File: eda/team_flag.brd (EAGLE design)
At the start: 40.6 x 40.6 mm, 28 parts, among them Q1 IRFML8244, Q2 IRFML8244, U1 ISL83491SOIC, U2 ATTINY1634

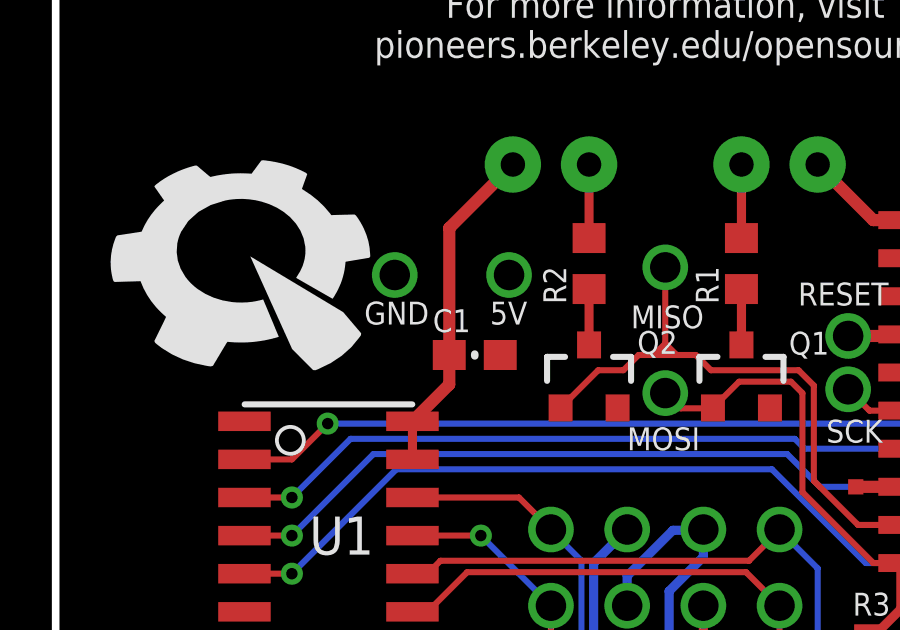
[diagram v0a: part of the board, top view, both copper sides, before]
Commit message: Replaced 2x4 connectors with 2x5's.
On smartsensor, smartsensorPowered, smartsensor_powered_jig, and team_flag.
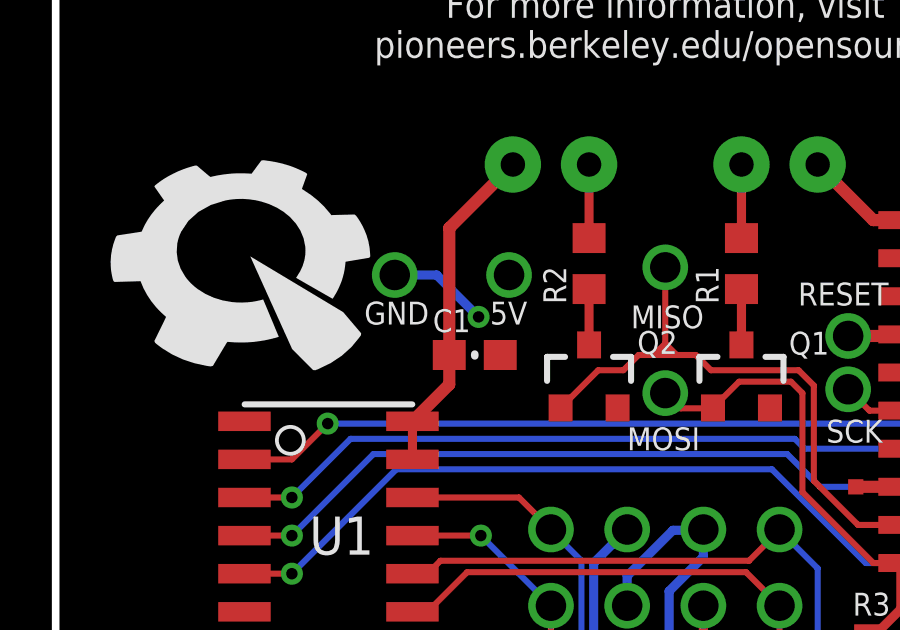
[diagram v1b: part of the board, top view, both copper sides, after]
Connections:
- net 5V: now also 5V.POGO_PIN
- net GND: now also GND.POGO_PIN
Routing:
- net GND: track 11.4 -> 14.9 mm, vias 0 -> 1
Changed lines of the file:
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@@
 <wire x1="17.018" y1="8.128" x2="18.0086" y2="8.128" width="0.3048" layer="16"/>
 <wire x1="18.0086" y1="8.128" x2="18.034" y2="8.1534" width="0.3048" layer="16"/>
-<wire x1="18.034" y1="2.794" x2="25.2594" y2="4.445" width="0" layer="19" extent="1-16"/>
+<contactref element="GND" pad="POGO_PIN"/>
+<wire x1="11.264" y1="13.97" x2="11.43" y2="13.97" width="0.3048" layer="1"/>
+<via x="10.541" y="15.24" extent="1-16" drill="0.381"/>
+<wire x1="7.747" y1="16.637" x2="9.144" y2="16.637" width="0.3048" layer="16"/>
+<wire x1="9.144" y1="16.637" x2="10.541" y2="15.24" width="0.3048" layer="16"/>
 </signal>
 <signal name="BLUE">
@@
 <wire x1="14.3764" y1="4.2672" x2="14.4018" y2="4.2926" width="0.3048" layer="16"/>
 <wire x1="14.3764" y1="7.0358" x2="15.494" y2="8.1534" width="0.3048" layer="16"/>
+<contactref element="5V" pad="POGO_PIN"/>
 </signal>
 <signal name="TX">

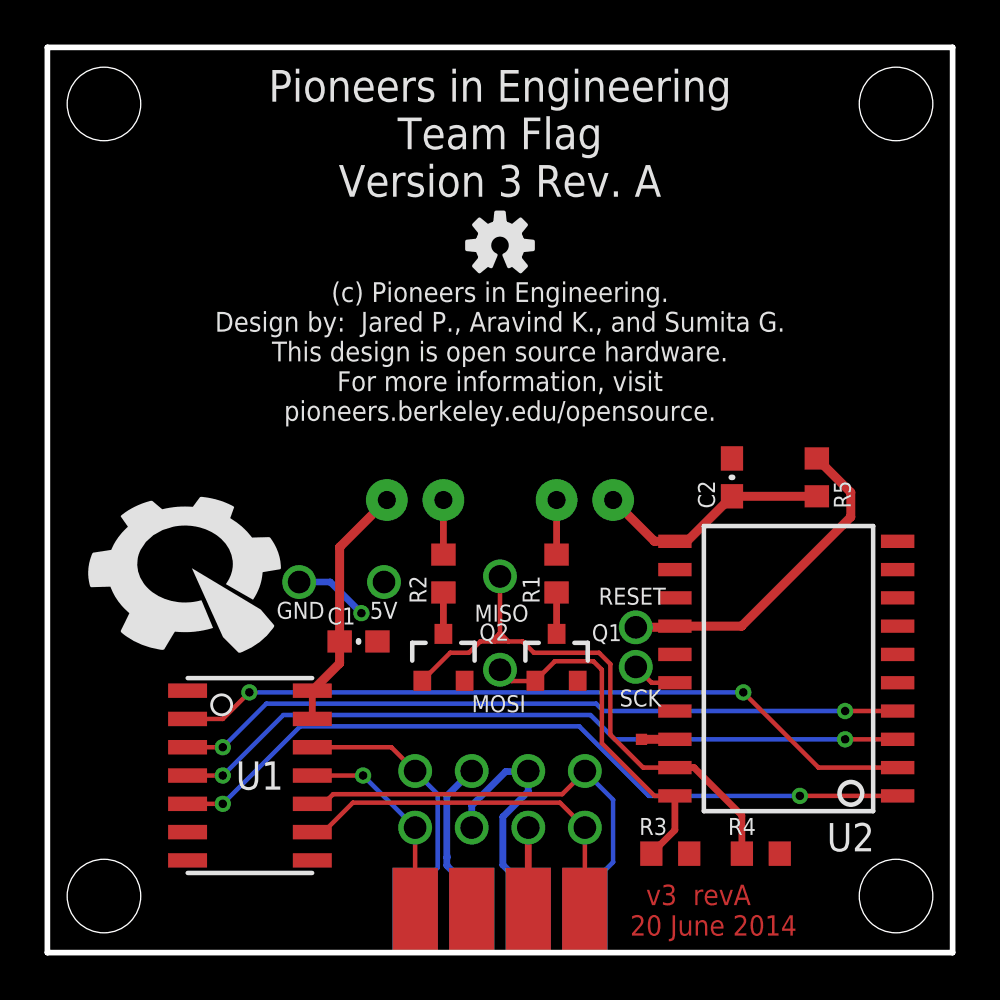
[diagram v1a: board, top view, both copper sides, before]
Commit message: Replaced 2x4 connector with 2x5 on team_flag.
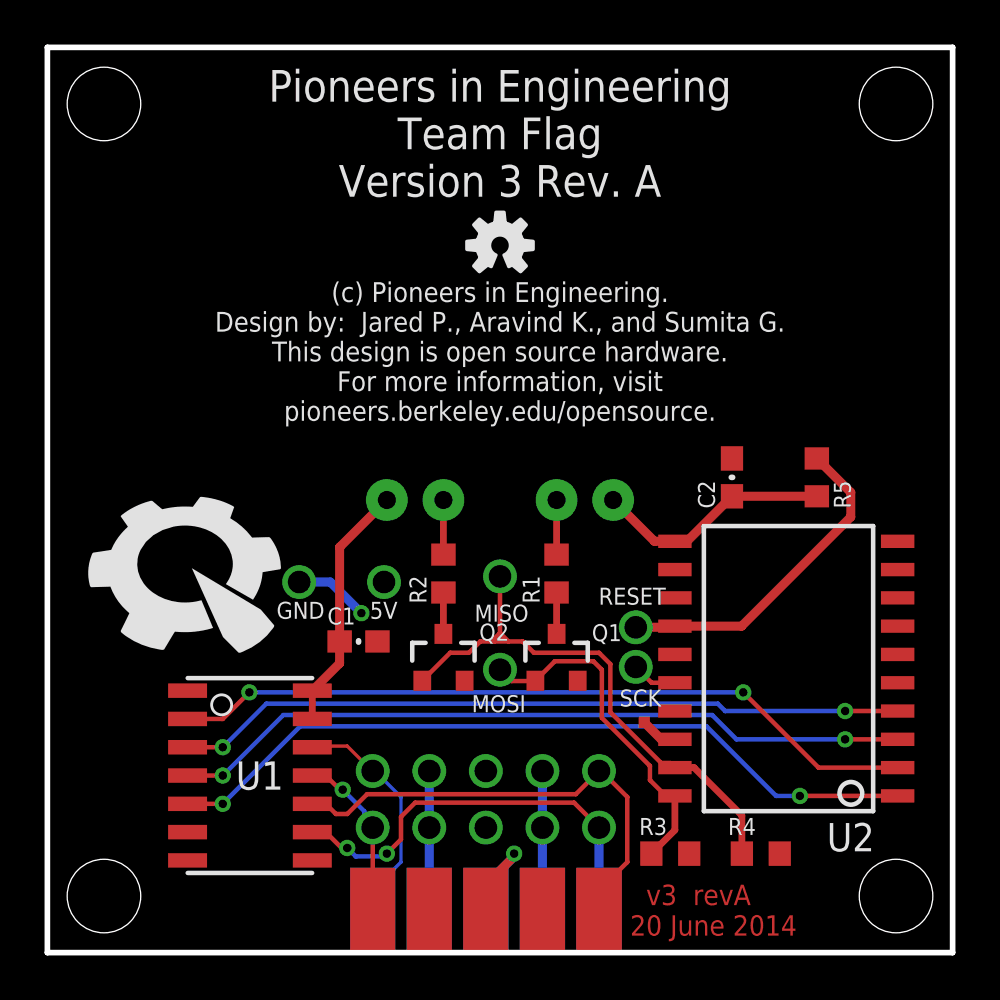
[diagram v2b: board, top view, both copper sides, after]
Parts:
- U$8: value SENSOR_CONPTH -> (none); device pie:2X4 -> pie:2X5
- U$9: value SENSOR_CONSMD-EDGE -> (none); device pie:2X4-EDGE -> pie:2X5-EDGE
- moved TP3 0.77 mm to (23.2, 10.3)
- moved U$8 0.63 mm to (16.1, 6.88)
- moved U$9 0.63 mm to (16.1, -0.64)
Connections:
- net 5V: now also U$8.5, U$9.5; no longer U$8.3, U$9.3
- net B_N: now also U$8.9, U$9.9; no longer U$8.7, U$9.7
- net B_P: now also U$8.10, U$9.10; no longer U$8.8, U$9.8
- net GND: now also U$8.3, U$8.7, U$8.8, U$9.3, U$9.7, U$9.8; no longer U$8.5, U$9.5
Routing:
- net 5V: track 32.9 -> 28.1 mm, vias 0 -> 1
- net B_P: track 17.0 -> 19.1 mm, vias 0 -> 2
- net A_N: track 9.29 -> 7.64 mm
- net A_P: track 12.1 -> 10.7 mm
- net B_N: track 20.2 -> 21.3 mm
- net GND: track 14.9 -> 16.0 mm
- net YELLOW: track 26.3 -> 25.7 mm
